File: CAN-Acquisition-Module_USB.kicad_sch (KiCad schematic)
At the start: 9 parts

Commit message: Added stuff and cleanup
Added LED, Power outputs, additional descriptions
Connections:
- net USB_ID renamed USB_OTG_ID
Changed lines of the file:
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@@
     (effects (font (size 1.27 1.27)) (justify left))
   )
-  (hierarchical_label "USB_ID" (shape input) (at 201.93 69.85 0)
+  (hierarchical_label "USB_OTG_ID" (shape output) (at 201.93 69.85 0)
     (effects (font (size 1.27 1.27)) (justify left))
   )
-  (hierarchical_label "USB_VBUS" (shape input) (at 201.93 59.69 0)
+  (hierarchical_label "USB_VBUS" (shape output) (at 201.93 59.69 0)
     (effects (font (size 1.27 1.27)) (justify left))
   )
-  (hierarchical_label "USB_D-" (shape input) (at 201.93 67.31 0)
+  (hierarchical_label "USB_D-" (shape bidirectional) (at 201.93 67.31 0)
     (effects (font (size 1.27 1.27)) (justify left))
   )
-  (hierarchical_label "USB_D+" (shape input) (at 201.93 64.77 0)
+  (hierarchical_label "USB_D+" (shape bidirectional) (at 201.93 64.77 0)
     (effects (font (size 1.27 1.27)) (justify left))
   )

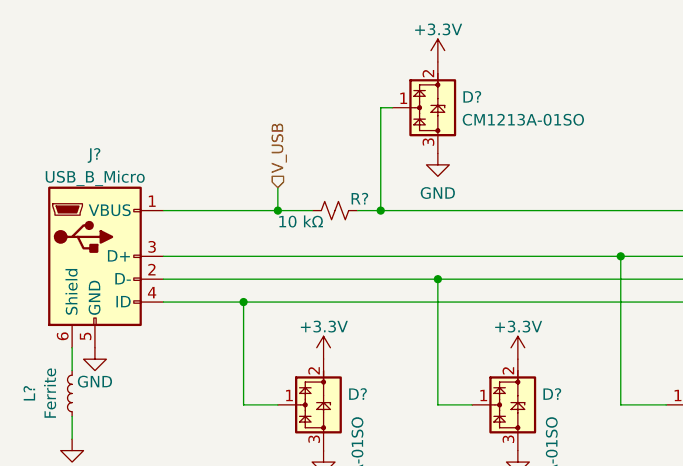
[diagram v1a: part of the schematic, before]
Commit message: Added analog and sensors sections
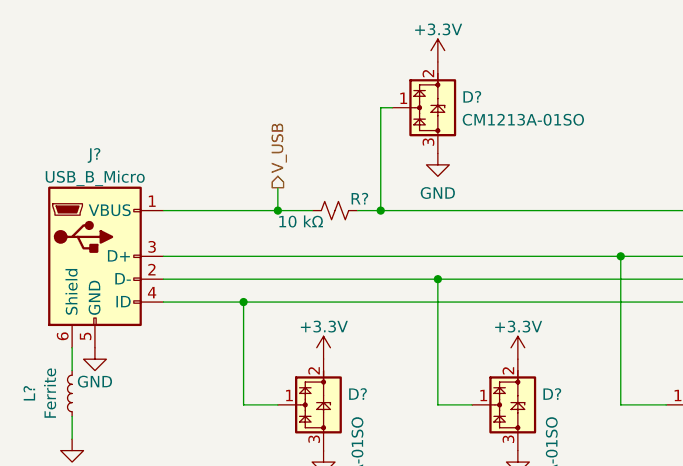
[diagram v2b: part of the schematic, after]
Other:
- company: (none) -> École de Technologie Supérieure - Laboratoire thermique et science du bâtiment (LTSB)
- title: (none) -> CANbus Acquisition Module
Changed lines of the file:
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@@
 (kicad_sch (version 20211123) (generator eeschema)
   (paper "A4")
+  (title_block
+    (title "CANbus Acquisition Module")
+    (date "2022-06-01")
+    (rev "A1")
+    (company "École de Technologie Supérieure - Laboratoire thermique et science du bâtiment (LTSB)")
+    (comment 1 "Designer: Hugo Boyce")
+  )
   (junction (at 128.27 67.31) (diameter 0) (color 0 0 0 0)
   )
@@
     (stroke (width 0) (type default) (color 0 0 0 0))
   )
-  (hierarchical_label "V_USB" (shape input) (at 110.49 57.15 90)
+  (hierarchical_label "V_USB" (shape output) (at 110.49 57.15 90)
     (effects (font (size 1.27 1.27)) (justify left))
   )

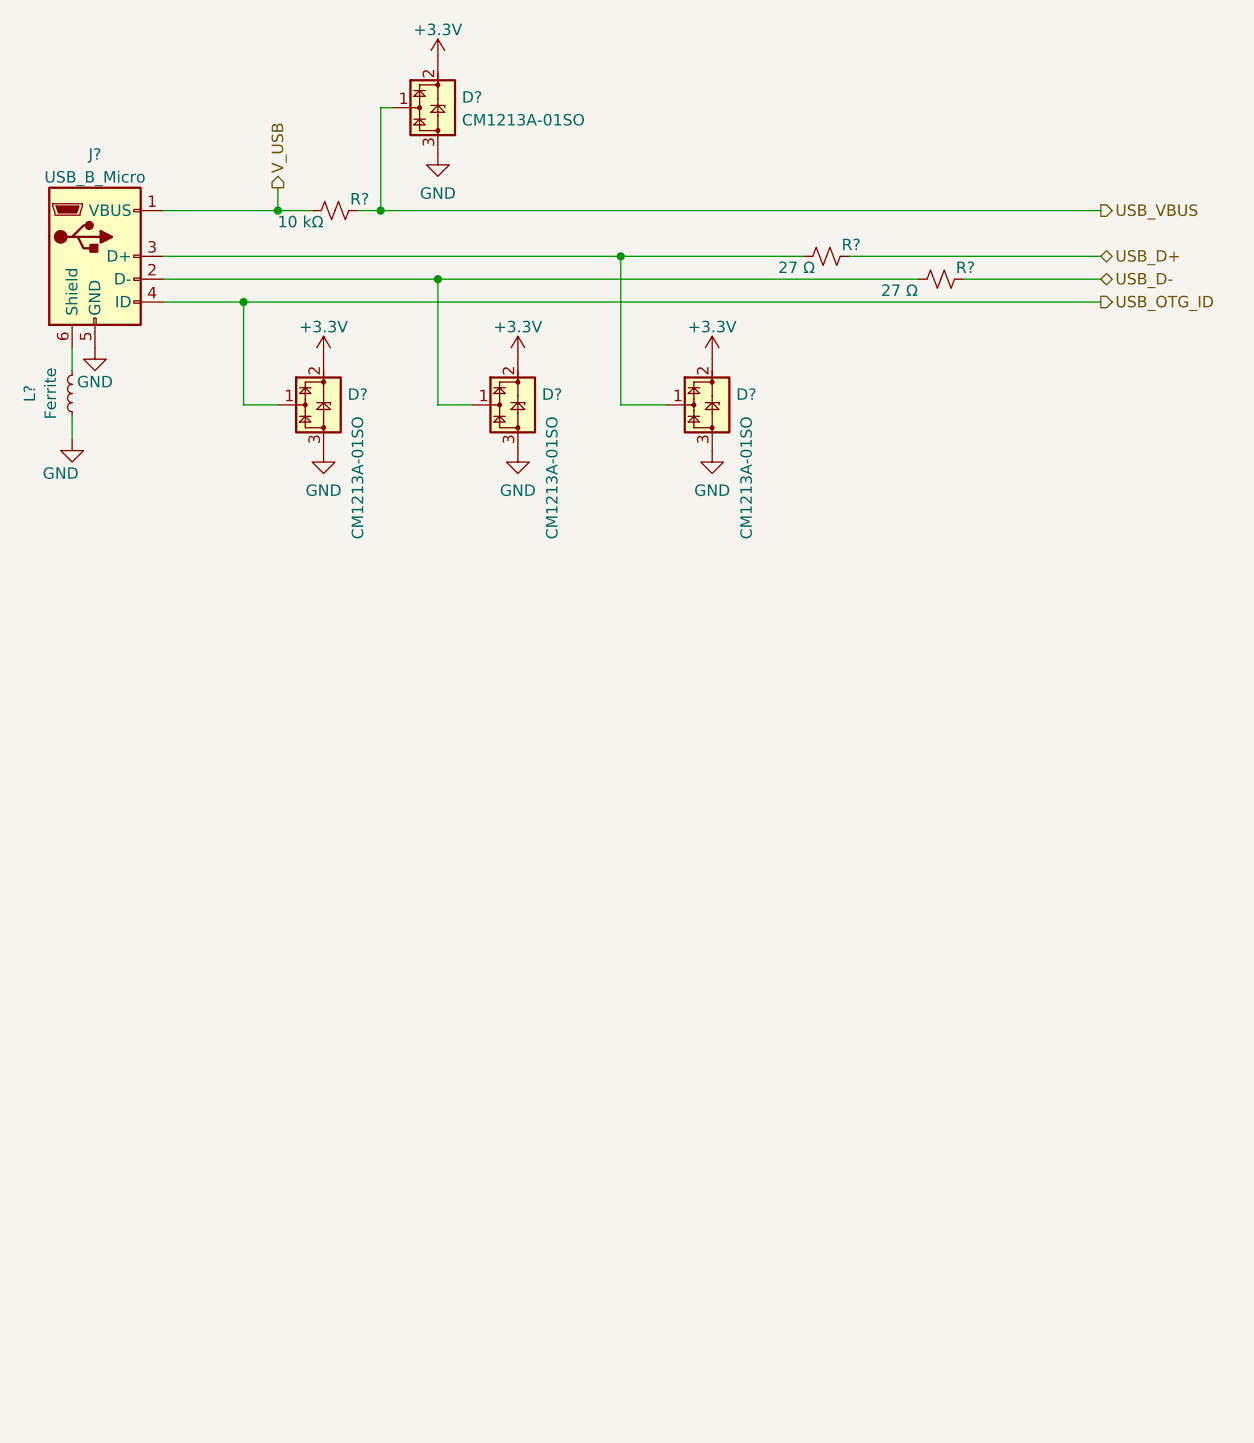
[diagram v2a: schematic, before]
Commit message: Added screen sections and annotations
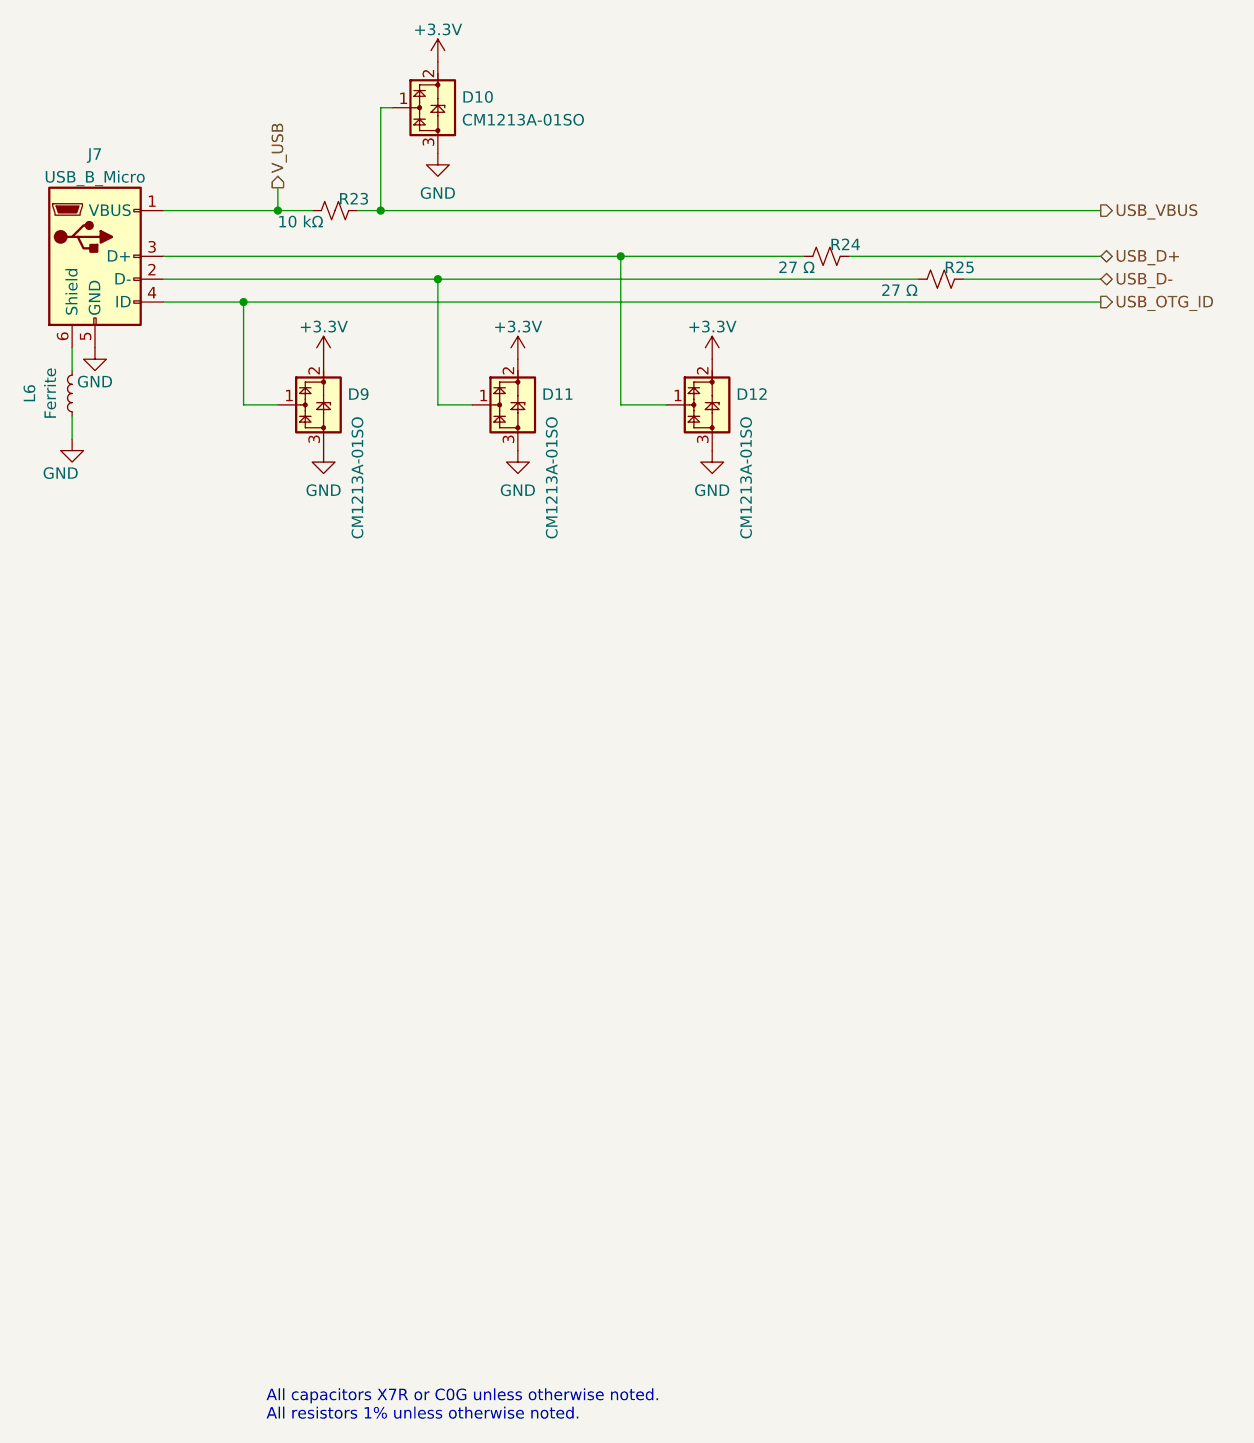
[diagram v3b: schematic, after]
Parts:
- gave numbers to parts that had none: 9
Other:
- note added: "All capacitors X7R or C0G unless otherwise noted. All resistors 1% unless otherwise noted."
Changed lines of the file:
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@@
     (stroke (width 0) (type default) (color 0 0 0 0))
   )
+  (text "All capacitors X7R or C0G unless otherwise noted.\nAll resistors 1% unless otherwise noted."
+    (at 109.22 194.31 0)
+    (effects (font (size 1.27 1.27)) (justify left bottom))
+  )
   (hierarchical_label "V_USB" (shape output) (at 110.49 57.15 90)
     (effects (font (size 1.27 1.27)) (justify left))
@@
   (symbol (lib_id "power:GND") (at 158.75 86.36 0) (unit 1)
     (in_bom yes) (on_board yes) (fields_autoplaced)
-    (property "Reference" "#PWR?" (id 0) (at 158.75 92.71 0)
+    (property "Reference" "#PWR085" (id 0) (at 158.75 92.71 0)
       (effects (font (size 1.27 1.27)) hide)
     )
@@
   (symbol (lib_id "power:+3.3V") (at 115.57 76.2 0) (unit 1)
     (in_bom yes) (on_board yes) (fields_autoplaced)
-    (property "Reference" "#PWR?" (id 0) (at 115.57 80.01 0)
+    (property "Reference" "#PWR078" (id 0) (at 115.57 80.01 0)
       (effects (font (size 1.27 1.27)) hide)
     )
@@
   (symbol (lib_id "power:GND") (at 90.17 74.93 0) (unit 1)
     (in_bom yes) (on_board yes)
-    (property "Reference" "#PWR?" (id 0) (at 90.17 81.28 0)
+    (property "Reference" "#PWR077" (id 0) (at 90.17 81.28 0)
       (effects (font (size 1.27 1.27)) hide)
     )
@@
   (symbol (lib_id "Device:L_Small") (at 87.63 80.01 180) (unit 1)
     (in_bom yes) (on_board yes)
-    (property "Reference" "L?" (id 0) (at 82.931 80.01 90))
+    (property "Reference" "L6" (id 0) (at 82.931 80.01 90))
     (property "Value" "Ferrite" (id 1) (at 85.2424 80.01 90))
     (property "Footprint" "Inductor_SMD:L_0603_1608Metric" (id 2) (at 87.63 80.01 0)
@@
   (symbol (lib_id "Power_Protection:CM1213A-01SO") (at 137.16 81.28 270) (unit 1)
     (in_bom yes) (on_board yes)
-    (property "Reference" "D?" (id 0) (at 139.827 80.1278 90)
+    (property "Reference" "D11" (id 0) (at 139.827 80.1278 90)
       (effects (font (size 1.27 1.27)) (justify left))
     )
@@
   (symbol (lib_id "Device:R_Small_US") (at 171.45 64.77 90) (unit 1)
     (in_bom yes) (on_board yes)
-    (property "Reference" "R?" (id 0) (at 175.26 63.5 90)
+    (property "Reference" "R24" (id 0) (at 175.26 63.5 90)
       (effects (font (size 1.27 1.27)) (justify left))
     )
@@
   (symbol (lib_id "power:+3.3V") (at 137.16 76.2 0) (unit 1)
     (in_bom yes) (on_board yes) (fields_autoplaced)
-    (property "Reference" "#PWR?" (id 0) (at 137.16 80.01 0)
+    (property "Reference" "#PWR082" (id 0) (at 137.16 80.01 0)
       (effects (font (size 1.27 1.27)) hide)
     )
@@
   (symbol (lib_id "power:+3.3V") (at 158.75 76.2 0) (unit 1)
     (in_bom yes) (on_board yes) (fields_autoplaced)
-    (property "Reference" "#PWR?" (id 0) (at 158.75 80.01 0)
+    (property "Reference" "#PWR084" (id 0) (at 158.75 80.01 0)
       (effects (font (size 1.27 1.27)) hide)
     )
@@
   (symbol (lib_id "Connector:USB_B_Micro") (at 90.17 64.77 0) (unit 1)
     (in_bom yes) (on_board yes) (fields_autoplaced)
-    (property "Reference" "J?" (id 0) (at 90.17 53.4502 0))
+    (property "Reference" "J7" (id 0) (at 90.17 53.4502 0))
     (property "Value" "USB_B_Micro" (id 1) (at 90.17 55.9871 0))
     (property "Footprint" "Connector_USB:USB_Micro-B_Wuerth_614105150721_Vertical" (id 2) (at 93.98 66.04 0)
@@
   (symbol (lib_id "Power_Protection:CM1213A-01SO") (at 158.75 81.28 270) (unit 1)
     (in_bom yes) (on_board yes)
-    (property "Reference" "D?" (id 0) (at 161.417 80.1278 90)
+    (property "Reference" "D12" (id 0) (at 161.417 80.1278 90)
       (effects (font (size 1.27 1.27)) (justify left))
     )
@@
   (symbol (lib_id "power:GND") (at 87.63 85.09 0) (unit 1)
     (in_bom yes) (on_board yes)
-    (property "Reference" "#PWR?" (id 0) (at 87.63 91.44 0)
+    (property "Reference" "#PWR076" (id 0) (at 87.63 91.44 0)
       (effects (font (size 1.27 1.27)) hide)
     )
@@
   (symbol (lib_id "Device:R_Small_US") (at 116.84 59.69 90) (unit 1)
     (in_bom yes) (on_board yes)
-    (property "Reference" "R?" (id 0) (at 120.65 58.42 90)
+    (property "Reference" "R23" (id 0) (at 120.65 58.42 90)
       (effects (font (size 1.27 1.27)) (justify left))
     )
@@
   (symbol (lib_id "power:+3.3V") (at 128.27 43.18 0) (unit 1)
     (in_bom yes) (on_board yes) (fields_autoplaced)
-    (property "Reference" "#PWR?" (id 0) (at 128.27 46.99 0)
+    (property "Reference" "#PWR080" (id 0) (at 128.27 46.99 0)
       (effects (font (size 1.27 1.27)) hide)
     )
@@
   (symbol (lib_id "power:GND") (at 137.16 86.36 0) (unit 1)
     (in_bom yes) (on_board yes) (fields_autoplaced)
-    (property "Reference" "#PWR?" (id 0) (at 137.16 92.71 0)
+    (property "Reference" "#PWR083" (id 0) (at 137.16 92.71 0)
       (effects (font (size 1.27 1.27)) hide)
     )
@@
   (symbol (lib_id "Power_Protection:CM1213A-01SO") (at 128.27 48.26 270) (unit 1)
     (in_bom yes) (on_board yes) (fields_autoplaced)
-    (property "Reference" "D?" (id 0) (at 130.937 47.1078 90)
+    (property "Reference" "D10" (id 0) (at 130.937 47.1078 90)
       (effects (font (size 1.27 1.27)) (justify left))
     )
@@
   (symbol (lib_id "Device:R_Small_US") (at 184.15 67.31 90) (unit 1)
     (in_bom yes) (on_board yes)
-    (property "Reference" "R?" (id 0) (at 187.96 66.04 90)
+    (property "Reference" "R25" (id 0) (at 187.96 66.04 90)
       (effects (font (size 1.27 1.27)) (justify left))
     )
@@
   (symbol (lib_id "power:GND") (at 115.57 86.36 0) (unit 1)
     (in_bom yes) (on_board yes) (fields_autoplaced)
-    (property "Reference" "#PWR?" (id 0) (at 115.57 92.71 0)
+    (property "Reference" "#PWR079" (id 0) (at 115.57 92.71 0)
       (effects (font (size 1.27 1.27)) hide)
     )
@@
   (symbol (lib_id "Power_Protection:CM1213A-01SO") (at 115.57 81.28 270) (unit 1)
     (in_bom yes) (on_board yes)
-    (property "Reference" "D?" (id 0) (at 118.237 80.1278 90)
+    (property "Reference" "D9" (id 0) (at 118.237 80.1278 90)
       (effects (font (size 1.27 1.27)) (justify left))
     )
@@
   (symbol (lib_id "power:GND") (at 128.27 53.34 0) (unit 1)
     (in_bom yes) (on_board yes) (fields_autoplaced)
-    (property "Reference" "#PWR?" (id 0) (at 128.27 59.69 0)
-      (effects (font (size 1.27 1.27)) hide)
-    )
+    (property "Reference" "#PWR081" (id 0) (at 128.27 59.69 0)
+      (effects (font (size 1.27 1.27)) hide)
+    )

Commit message: PCB started
Placement well advanced
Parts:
- J7: footprint Connector_USB:USB_Micro-B_Wuerth_614105150721_Vertical -> CAN-Acquisition-Module:GCT-USB3131-30-0230-A; Alternate Mfr. GCT -> (none); Alternate P/N USB3131-30-0230-A -> (none); Mfr. (none) -> GCT; P/N (none) -> USB3131-30-0230-A
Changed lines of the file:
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@@
     (property "Reference" "J7" (id 0) (at 90.17 53.4502 0))
     (property "Value" "USB_B_Micro" (id 1) (at 90.17 55.9871 0))
-    (property "Footprint" "Connector_USB:USB_Micro-B_Wuerth_614105150721_Vertical" (id 2) (at 93.98 66.04 0)
+    (property "Footprint" "CAN-Acquisition-Module:GCT-USB3131-30-0230-A" (id 2) (at 93.98 66.04 0)
       (effects (font (size 1.27 1.27)) hide)
     )
@@
       (effects (font (size 1.27 1.27)) hide)
     )
-    (property "Alternate Mfr." "GCT" (id 4) (at 90.17 64.77 0)
+    (property "Mfr." "GCT" (id 4) (at 90.17 64.77 0)
       (effects (font (size 1.27 1.27)) hide)
     )
-    (property "Alternate P/N" "USB3131-30-0230-A" (id 5) (at 90.17 64.77 0)
+    (property "P/N" "USB3131-30-0230-A" (id 5) (at 90.17 64.77 0)
       (effects (font (size 1.27 1.27)) hide)
     )
